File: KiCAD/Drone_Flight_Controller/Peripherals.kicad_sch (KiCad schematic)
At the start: 65 parts, among them J1 XT60, J2 0.5mΩ high side shunt, Q1 2N2222A, U1 74AHC1G125, U2 74AHC1G125, U3 74AHC1G125, U4 74AHC1G125, U9 INA195

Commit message: Routing and placing
Routing and placing
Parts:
- removed D14, D16, D17, D18: LED, LED_SMD:LED_0805_2012Metric_Pad1.15x1.40mm_HandSolder, symbol Device:LED
- removed R20, R21, R22, R23: 3k6, Resistor_SMD:R_0805_2012Metric_Pad1.20x1.40mm_HandSolder, symbol Device:R

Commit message: Revision
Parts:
- renumbered 3V1 to 3V3
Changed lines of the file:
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@@
 		(dnp no)
 		(fields_autoplaced yes)
-		(property "Reference" "3V1"
+		(property "Reference" "3V3"
 			(at 93.98 120.6499 90)
 			(effects
@@
 			(project "Drone_Flight_Controller"
 				(path "/51ab9491-7068-4b24-bb38-47a0c739796e/a1832adb-c070-4778-a5ef-97ea378c06da"
-					(reference "3V1")
+					(reference "3V3")
 					(unit 1)
 				)
@@
 		(fields_autoplaced yes)
 		(property "Reference" "GND1"
-			(at 93.98 116.205 90)
+			(at 93.98 115.5699 90)
 			(effects
 				(font
@@
 		)
 		(property "Value" "GND"
-			(at 93.98 118.745 90)
-			(effects
-				(font
+			(at 93.98 118.1099 90)
+			(effects
+				(font

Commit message: Add signage
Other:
- note added: "Video"
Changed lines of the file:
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@@
+		)
+	)
+	(text "Video"
+		(exclude_from_sim no)
+		(at 45.974 149.098 0)
+		(effects
+			(font
+				(size 1.27 1.27)
+			)
 		)
 	)

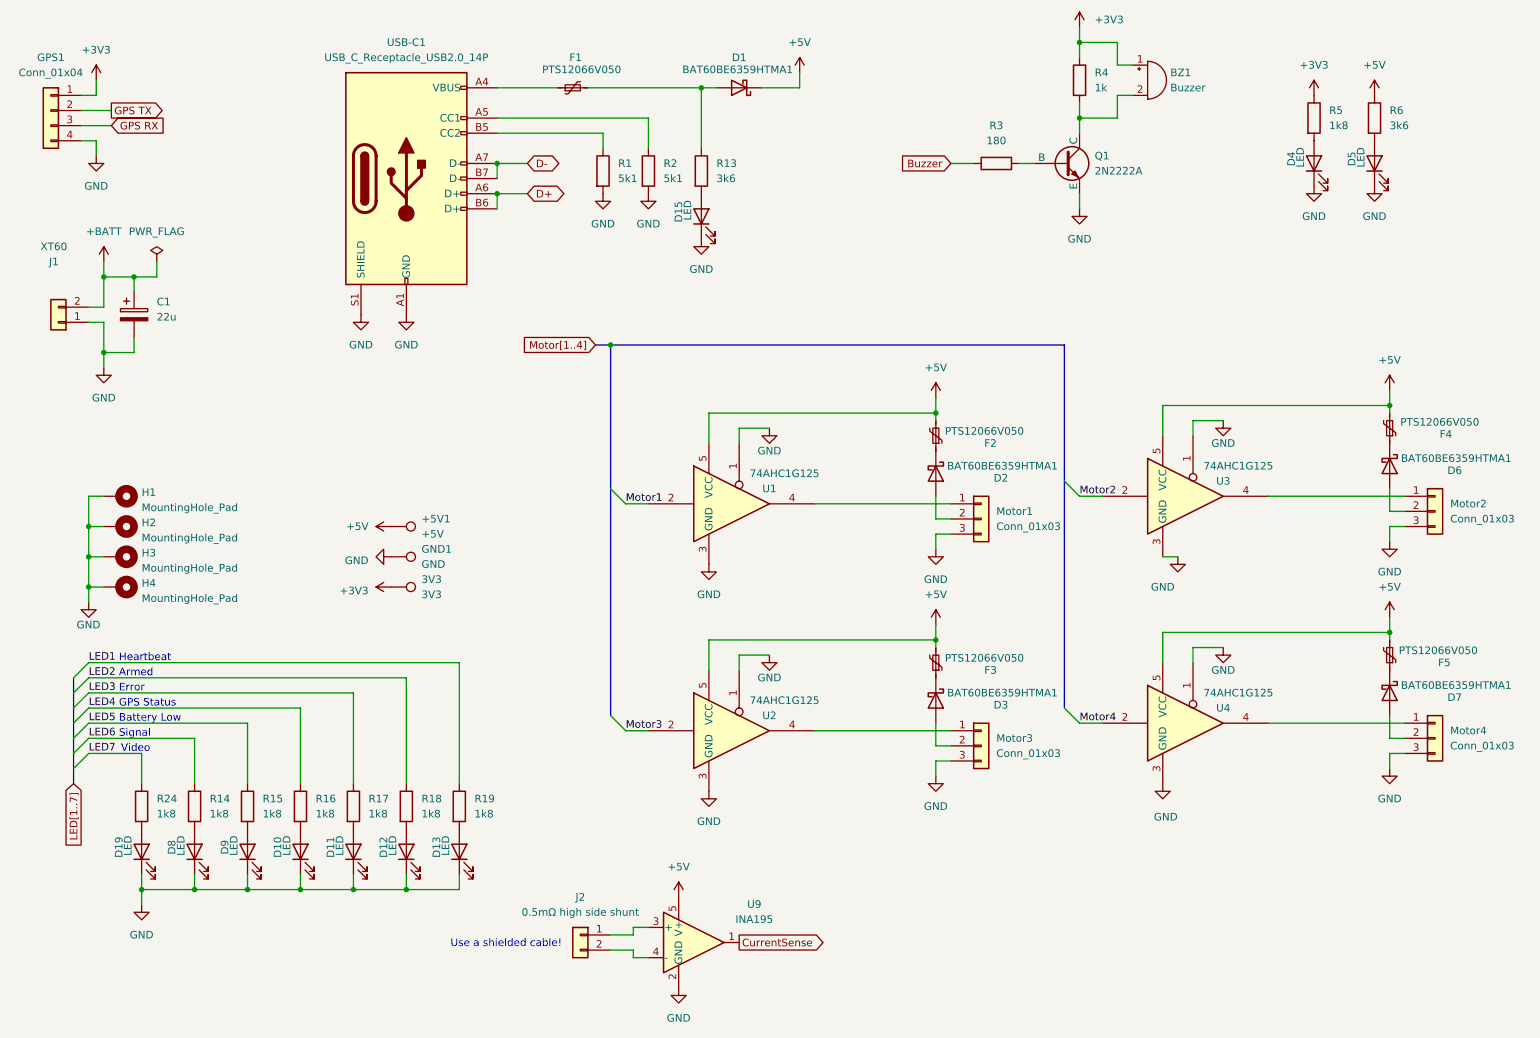
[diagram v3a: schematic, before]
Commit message: Mark GND on connectors
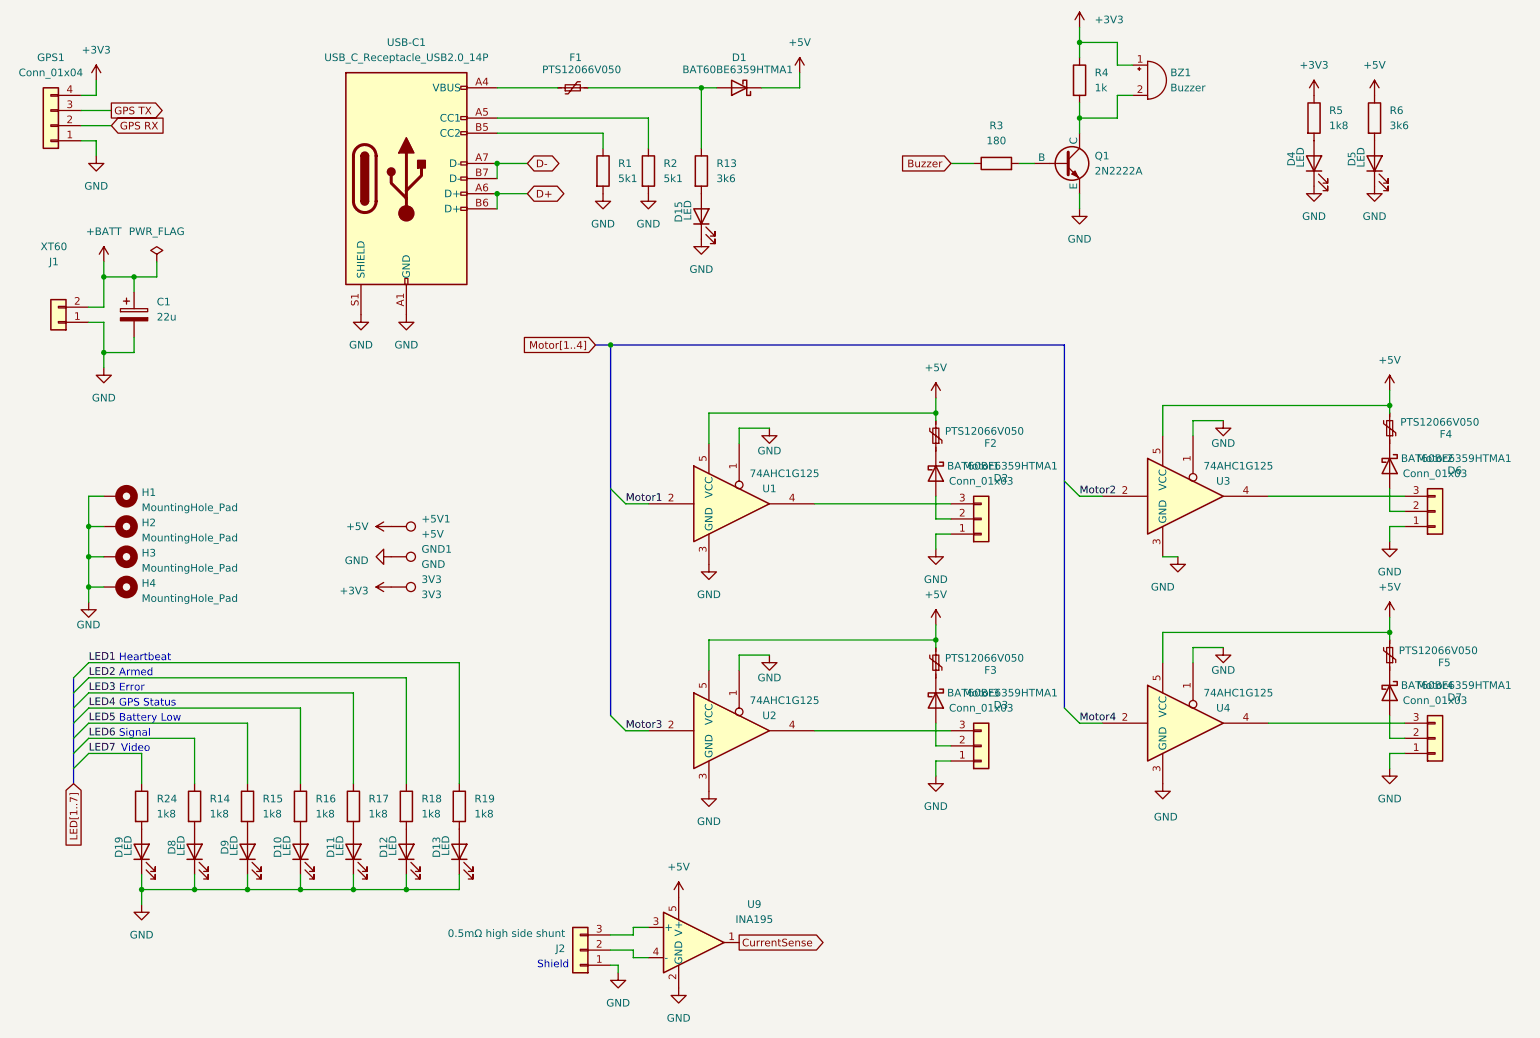
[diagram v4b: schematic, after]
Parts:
- removed J2: 0.5mΩ high side shunt, Connector_PinHeader_2.54mm:PinHeader_1x02_P2.54mm_Vertical, symbol Connector_Generic:Conn_01x02
- added J2: 0.5mΩ high side shunt, Connector_PinHeader_2.54mm:PinHeader_1x03_P2.54mm_Vertical, symbol Connector_Generic:Conn_01x03
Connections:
- net +3V3: now also GPS1.4 (Pin_4); no longer GPS1.1 (Pin_1)
- net GND: now also GPS1.1 (Pin_1), Motor1.1 (Pin_1), Motor2.1 (Pin_1), Motor3.1 (Pin_1), Motor4.1 (Pin_1), J2.1 (Pin_1); no longer GPS1.4 (Pin_4), Motor1.3 (Pin_3), Motor2.3 (Pin_3), Motor3.3 (Pin_3), Motor4.3 (Pin_3)
- net GPS RX: now also GPS1.2 (Pin_2); no longer GPS1.3 (Pin_3)
- net GPS TX: now also GPS1.3 (Pin_3); no longer GPS1.2 (Pin_2)
- net at U4.4: now also Motor4.3 (Pin_3); no longer Motor4.1 (Pin_1)
- net at U9.3 (+): now also J2.3 (Pin_3)
- net at U9.4 (-): now also J2.2 (Pin_2)
- net at U1.4: now also Motor1.3 (Pin_3); no longer Motor1.1 (Pin_1)
- net at U3.4: now also Motor2.3 (Pin_3); no longer Motor2.1 (Pin_1)
- net at U2.4: now also Motor3.3 (Pin_3); no longer Motor3.1 (Pin_1)
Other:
- note added: "Shield"
- note removed: "Use a shielded cable!"
- moved on the sheet: GPS1
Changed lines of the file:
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@@
 		)
 	)
-	(text "Use a shielded cable!"
+	(text "Video"
 		(exclude_from_sim no)
-		(at 108.204 181.864 0)
+		(at 45.974 149.098 0)
 		(effects
 			(font
@@
 		)
 	)
-	(text "Video"
+	(text "Error"
 		(exclude_from_sim no)
-		(at 45.974 149.098 0)
+		(at 43.18 138.938 0)
 		(effects
 			(font
 				(size 1.27 1.27)
 			)
+			(justify left)
 		)
 	)
-	(text "Error"
+	(text "Shield"
 		(exclude_from_sim no)
-		(at 43.18 138.938 0)
+		(at 116.078 185.42 0)
 		(effects
 			(font
 				(size 1.27 1.27)
 			)
-			(justify left)
 		)
 	)
@@
 	(wire
 		(pts
+			(xy 127 186.69) (xy 127 185.42)
+		)
+		(stroke
+			(width 0)
+			(type default)
+		)
+	)
+	(wire
+		(pts
 			(xy 39.37 36.83) (xy 39.37 39.37)
 		)
@@
 	(wire
 		(pts
+			(xy 127 185.42) (xy 125.73 185.42)
+		)
+		(stroke
+			(width 0)
+			(type default)
+		)
+	)
+	(wire
+		(pts
 			(xy 40.64 82.55) (xy 40.64 85.09)
 		)
@@
 		(lib_id "Connector_Generic:Conn_01x03")
 		(at 264.16 147.32 0)
+		(mirror x)
 		(unit 1)
 		(exclude_from_sim no)
@@
 		(on_board yes)
 		(dnp no)
-		(fields_autoplaced yes)
 		(property "Reference" "Motor4"
-			(at 266.7 146.0499 0)
+			(at 264.16 138.43 0)
 			(effects
 				(font
 					(size 1.27 1.27)
 				)
-				(justify left)
 			)
 		)
 		(property "Value" "Conn_01x03"
-			(at 266.7 148.5899 0)
+			(at 264.16 140.97 0)
 			(effects
 				(font
 					(size 1.27 1.27)
 				)
-				(justify left)
 			)
 		)
@@
 		(lib_id "Connector_Generic:Conn_01x03")
 		(at 187.96 110.49 0)
+		(mirror x)
 		(unit 1)
 		(exclude_from_sim no)
@@
 		(on_board yes)
 		(dnp no)
-		(fields_autoplaced yes)
 		(property "Reference" "Motor1"
-			(at 190.5 109.2199 0)
+			(at 187.96 101.6 0)
 			(effects
 				(font
 					(size 1.27 1.27)
 				)
-				(justify left)
 			)
 		)
 		(property "Value" "Conn_01x03"
-			(at 190.5 111.7599 0)
+			(at 187.96 104.14 0)
 			(effects
 				(font
 					(size 1.27 1.27)
 				)
-				(justify left)
 			)
 		)
@@
 	(symbol
 		(lib_id "power:GND")
+		(at 127 186.69 0)
+		(unit 1)
+		(exclude_from_sim no)
+		(in_bom yes)
+		(on_board yes)
+		(dnp no)
+		(fields_autoplaced yes)
+		(property "Reference" "#PWR062"
+			(at 127 193.04 0)
+			(effects
+				(font
+					(size 1.27 1.27)
+				)
+				(hide yes)
+			)
+		)
+		(property "Value" "GND"
+			(at 127 191.77 0)
+			(effects
+				(font
+					(size 1.27 1.27)
+				)
+			)
+		)
+		(property "Footprint" ""
+			(at 127 186.69 0)
+			(effects
+				(font
+					(size 1.27 1.27)
+				)
+				(hide yes)
+			)
+		)
+		(property "Datasheet" ""
+			(at 127 186.69 0)
+			(effects
+				(font
+					(size 1.27 1.27)
+				)
+				(hide yes)
+			)
+		)
+		(property "Description" "Power symbol creates a global label with name \"GND\" , ground"
+			(at 127 186.69 0)
+			(effects
+				(font
+					(size 1.27 1.27)
+				)
+				(hide yes)
+			)
+		)
+		(pin "1"
+		)
+		(instances
+			(project ""
+				(path "/51ab9491-7068-4b24-bb38-47a0c739796e/a1832adb-c070-4778-a5ef-97ea378c06da"
+					(reference "#PWR062")
+					(unit 1)
+				)
+			)
+		)
+	)
+	(symbol
+		(lib_id "power:GND")
 		(at 243.84 54.61 0)
 		(unit 1)
@@
 	)
 	(symbol
+		(lib_id "Connector_Generic:Conn_01x03")
+		(at 120.65 182.88 180)
+		(unit 1)
+		(exclude_from_sim no)
+		(in_bom yes)
+		(on_board yes)
+		(dnp no)
+		(property "Reference" "J2"
+			(at 118.11 182.626 0)
+			(effects
+				(font
+					(size 1.27 1.27)
+				)
+				(justify left)
+			)
+		)
+		(property "Value" "0.5mΩ high side shunt"
+			(at 118.11 180.086 0)
+			(effects
+				(font
+					(size 1.27 1.27)
+				)
+				(justify left)
+			)
+		)
+		(property "Footprint" "Connector_PinHeader_2.54mm:PinHeader_1x03_P2.54mm_Vertical"
+			(at 120.65 182.88 0)
+			(effects
+				(font
+					(size 1.27 1.27)
+				)
+				(hide yes)
+			)
+		)
+		(property "Datasheet" "~"
+			(at 120.65 182.88 0)
+			(effects
+				(font
+					(size 1.27 1.27)
+				)
+				(hide yes)
+			)
+		)
+		(property "Description" "Generic connector, single row, 01x03, script generated (kicad-library-utils/schlib/autogen/connector/)"
+			(at 120.65 182.88 0)
+			(effects
+				(font
+					(size 1.27 1.27)
+				)
+				(hide yes)
+			)
+		)
+		(pin "3"
+		)
+		(pin "2"
+		)
+		(pin "1"
+		)
+		(instances
+			(project "Drone_Flight_Controller"
+				(path "/51ab9491-7068-4b24-bb38-47a0c739796e/a1832adb-c070-4778-a5ef-97ea378c06da"
+					(reference "J2")
+					(unit 1)
+				)
+			)
+		)
+	)
+	(symbol
 		(lib_id "Device:C_Polarized")
 		(at 45.72 76.2 0)
@@
 	(symbol
 		(lib_id "Connector_Generic:Conn_01x04")
-		(at 31.75 41.91 0)
-		(mirror y)
+		(at 31.75 44.45 180)
 		(unit 1)
 		(exclude_from_sim no)
@@
 		(on_board yes)
 		(dnp no)
-		(fields_autoplaced yes)
 		(property "Reference" "GPS1"
 			(at 31.75 33.02 0)
@@
 		)
 		(property "Footprint" "Connector_PinHeader_2.54mm:PinHeader_1x04_P2.54mm_Vertical"
-			(at 31.75 41.91 0)
+			(at 31.75 44.45 0)
 			(effects
 				(font
@@
 		)
 		(property "Datasheet" "/"
-			(at 31.75 41.91 0)
+			(at 31.75 44.45 0)
 			(effects
 				(font
@@
 		)
 		(property "Description" "Generic connector, single row, 01x04, script generated (kicad-library-utils/schlib/autogen/connector/)"
-			(at 31.75 41.91 0)
+			(at 31.75 44.45 0)
 			(effects
 				(font
@@
 		)
 		(property "Link" "/"
-			(at 31.75 41.91 0)
+			(at 31.75 44.45 0)
 			(effects
 				(font
@@
 	)
 	(symbol
-		(lib_id "Connector_Generic:Conn_01x02")
-		(at 120.65 180.34 0)
-		(mirror y)
-		(unit 1)
-		(exclude_from_sim no)
-		(in_bom yes)
-		(on_board yes)
-		(dnp no)
-		(fields_autoplaced yes)
-		(property "Reference" "J2"
-			(at 120.65 173.99 0)
-			(effects
-				(font
-					(size 1.27 1.27)
-				)
-			)
-		)
-		(property "Value" "0.5mΩ high side shunt"
-			(at 120.65 176.53 0)
-			(effects
-				(font
-					(size 1.27 1.27)
-				)
-			)
-		)
-		(property "Footprint" "Connector_PinHeader_2.54mm:PinHeader_1x02_P2.54mm_Vertical"
-			(at 120.65 180.34 0)
-			(effects
-				(font
-					(size 1.27 1.27)
-				)
-				(hide yes)
-			)
-		)
-		(property "Datasheet" "~"
-			(at 120.65 180.34 0)
-			(effects
-				(font
-					(size 1.27 1.27)
-				)
-				(hide yes)
-			)
-		)
-		(property "Description" "Generic connector, single row, 01x02, script generated (kicad-library-utils/schlib/autogen/connector/)"
-			(at 120.65 180.34 0)
-			(effects
-				(font
-					(size 1.27 1.27)
-				)
-				(hide yes)
-			)
-		)
-		(pin "1"
-		)
-		(pin "2"
-		)
-		(instances
-			(project ""
-				(path "/51ab9491-7068-4b24-bb38-47a0c739796e/a1832adb-c070-4778-a5ef-97ea378c06da"
-					(reference "J2")
-					(unit 1)
-				)
-			)
-		)
-	)
-	(symbol
 		(lib_id "Connector_Generic:Conn_01x03")
 		(at 264.16 109.22 0)
+		(mirror x)
 		(unit 1)
 		(exclude_from_sim no)
@@
 		(on_board yes)
 		(dnp no)
-		(fields_autoplaced yes)
 		(property "Reference" "Motor2"
-			(at 266.7 107.9499 0)
+			(at 264.16 100.33 0)
 			(effects
 				(font
 					(size 1.27 1.27)
 				)
-				(justify left)
 			)
 		)
 		(property "Value" "Conn_01x03"
-			(at 266.7 110.4899 0)
+			(at 264.16 102.87 0)
 			(effects
 				(font
 					(size 1.27 1.27)
 				)
-				(justify left)
 			)
 		)
@@
 		(lib_id "Connector_Generic:Conn_01x03")
 		(at 187.96 148.59 0)
+		(mirror x)
 		(unit 1)
 		(exclude_from_sim no)
@@
 		(on_board yes)
 		(dnp no)
-		(fields_autoplaced yes)
 		(property "Reference" "Motor3"
-			(at 190.5 147.3199 0)
+			(at 187.96 139.7 0)
 			(effects
 				(font
 					(size 1.27 1.27)
 				)
-				(justify left)
 			)
 		)
 		(property "Value" "Conn_01x03"
-			(at 190.5 149.8599 0)
+			(at 187.96 142.24 0)
 			(effects
 				(font
 					(size 1.27 1.27)
 				)
-				(justify left)
 			)
 		)
